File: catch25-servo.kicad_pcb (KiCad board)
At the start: 2 copper layers, 1 part

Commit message: update files
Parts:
- added C1: 10u, Capacitor_SMD:C_0603_1608Metric_Pad1.08x0.95mm_HandSolder, F.Cu at (152.5, 117.5)
- added C2: 22u, Capacitor_SMD:C_0603_1608Metric_Pad1.08x0.95mm_HandSolder, F.Cu at (171.0, 122.5)
- added C3: 10u, Capacitor_SMD:C_0603_1608Metric_Pad1.08x0.95mm_HandSolder, F.Cu at (168.0, 107.0)
- added C4: 10u, Capacitor_SMD:C_0603_1608Metric_Pad1.08x0.95mm_HandSolder, F.Cu at (168.0, 98.5)
- added C5: 0.1u, Capacitor_SMD:C_0603_1608Metric_Pad1.08x0.95mm_HandSolder, F.Cu at (163.0, 97.0)
- added D1: 1N4148, Diode_THT:D_DO-35_SOD27_P7.62mm_Horizontal, F.Cu at (164.5, 106.5)
- added J1: Conn_01x03, Connector_Molex:Molex_SPOX_5268-03A_1x03_P2.50mm_Horizontal, F.Cu at (154.0, 87.6)
- added J2: Conn_01x03, Connector_Molex:Molex_SPOX_5268-03A_1x03_P2.50mm_Horizontal, F.Cu at (165.0, 87.6)
- added J3: Conn_02x05_Odd_Even, Connector_PinSocket_2.54mm:PinSocket_2x05_P2.54mm_Horizontal, F.Cu at (134.4, 85.9)
- added J4: Conn_01x06, Connector_PinSocket_2.54mm:PinSocket_1x06_P2.54mm_Vertical, F.Cu at (131.9, 83.0)
- added J5: Conn_01x02, Connector_AMASS:AMASS_XT30PW-M_1x02_P2.50mm_Horizontal, F.Cu at (158.0, 130.3)
- added Q1: 2N3906, Package_TO_SOT_THT:TO-92_Inline, F.Cu at (157.0, 101.0)
- added R2: 1.2k, Resistor_SMD:R_0603_1608Metric_Pad0.98x0.95mm_HandSolder, F.Cu at (156.5, 109.5)
- added R3: 10k, Resistor_SMD:R_0603_1608Metric_Pad0.98x0.95mm_HandSolder, F.Cu at (158.5, 105.6)
- added R4: 10k, Resistor_SMD:R_0603_1608Metric_Pad0.98x0.95mm_HandSolder, F.Cu at (160.5, 105.6)
- added R5: 10k, Resistor_SMD:R_0603_1608Metric_Pad0.98x0.95mm_HandSolder, F.Cu at (167.3, 95.5)
- added R6: 10k, Resistor_SMD:R_0603_1608Metric_Pad0.98x0.95mm_HandSolder, F.Cu at (167.3, 91.5)
- added R7: 10k, Resistor_SMD:R_0603_1608Metric_Pad0.98x0.95mm_HandSolder, F.Cu at (167.3, 93.5)
- added U1: ~, Package_SO:VSSOP-8_2.3x2mm_P0.5mm, F.Cu at (160.7, 95.0)
- added U2: MC78L05_SOT89, Package_TO_SOT_SMD:SOT-89-3, F.Cu at (169.0, 103.0)
- moved MD1 148.2 mm to (162.0, 118.5), turned to 180 degrees
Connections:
- MD1 pad 1: unconnected-(MD1-~{ON}/OFF_CONTROL-Pad1) -> GND
- MD1 pad 2: unconnected-(MD1-VIN-Pad2) -> +BATT
- MD1 pad 3: unconnected-(MD1-1_GROUND-Pad3) -> GND
- MD1 pad 4: unconnected-(MD1-VOUT-Pad4) -> VCC
- MD1 pad 5: unconnected-(MD1-SENSE-Pad5) -> VCC
- MD1 pad 6: unconnected-(MD1-TRIM-Pad6) -> Net-(MD1-TRIM)
- MD1 pad 7: unconnected-(MD1-2_GROUND-Pad7) -> GND
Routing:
- net +5V: track 0.00 -> 61.2 mm, vias 0 -> 1
- net /UART_TX: track 0.00 -> 51.9 mm, vias 0 -> 2
- net /UART_RX: track 0.00 -> 42.8 mm
- net GND: track 0.00 -> 41.3 mm
- net +BATT: track 0.00 -> 38.3 mm
- net /SERVO_SIG: track 0.00 -> 31.7 mm
- net /TXEN: track 0.00 -> 23.0 mm, vias 0 -> 2
- net VCC: track 0.00 -> 7.72 mm
- net Net-(Q1-B): track 0.00 -> 3.84 mm
- net Net-(MD1-TRIM): track 0.00 -> 3.62 mm
- added copper zone on B.Cu, net GND
- added copper zone on F.Cu, net GND
- added copper zone on B.Cu, net VCC
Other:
- board outline added: 41.5 x 64 mm
- board text added: "FE-IP-1"
- board text added: "IP:192.168."
- board text added: "JLCJLCJLCJLC"

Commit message: update files
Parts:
- added D2: SMAJ45CA, Diode_SMD:D_SMA_Handsoldering, F.Cu at (161.5, 128.0)
- moved C2 3.04 mm to (170.5, 125.5), turned to -90 degrees
- moved J5 1.68 mm to (158.0, 132.0)
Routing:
- net GND: track 41.3 -> 65.8 mm, vias 0 -> 48
- net +BATT: track 38.3 -> 44.8 mm
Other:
- board size 41.5 x 64 mm -> 41.5 x 65 mm

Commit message: update resources
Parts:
- removed U2: MC78L05_SOT89, Package_TO_SOT_SMD:SOT-89-3
- added U3: AMS1117-5.0, Package_TO_SOT_SMD:SOT-223-3_TabPin2, F.Cu at (166.5, 103.0)
- C2: footprint Capacitor_SMD:C_0603_1608Metric_Pad1.08x0.95mm_HandSolder -> Capacitor_SMD:C_0805_2012Metric_Pad1.18x1.45mm_HandSolder
- moved C3 7.65 mm to (160.5, 105.5), turned to -90 degrees
- moved D1 3.03 mm to (162.2, 108.5), turned to 0 degrees
- moved R4 1.51 mm to (159.0, 105.5)
- moved R3 1.01 mm to (157.5, 105.5)
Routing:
- net +5V: track 61.2 -> 75.7 mm
- net +BATT: track 44.8 -> 49.7 mm
- net /UART_TX: track 51.9 -> 50.9 mm
- net GND: vias 48 -> 51

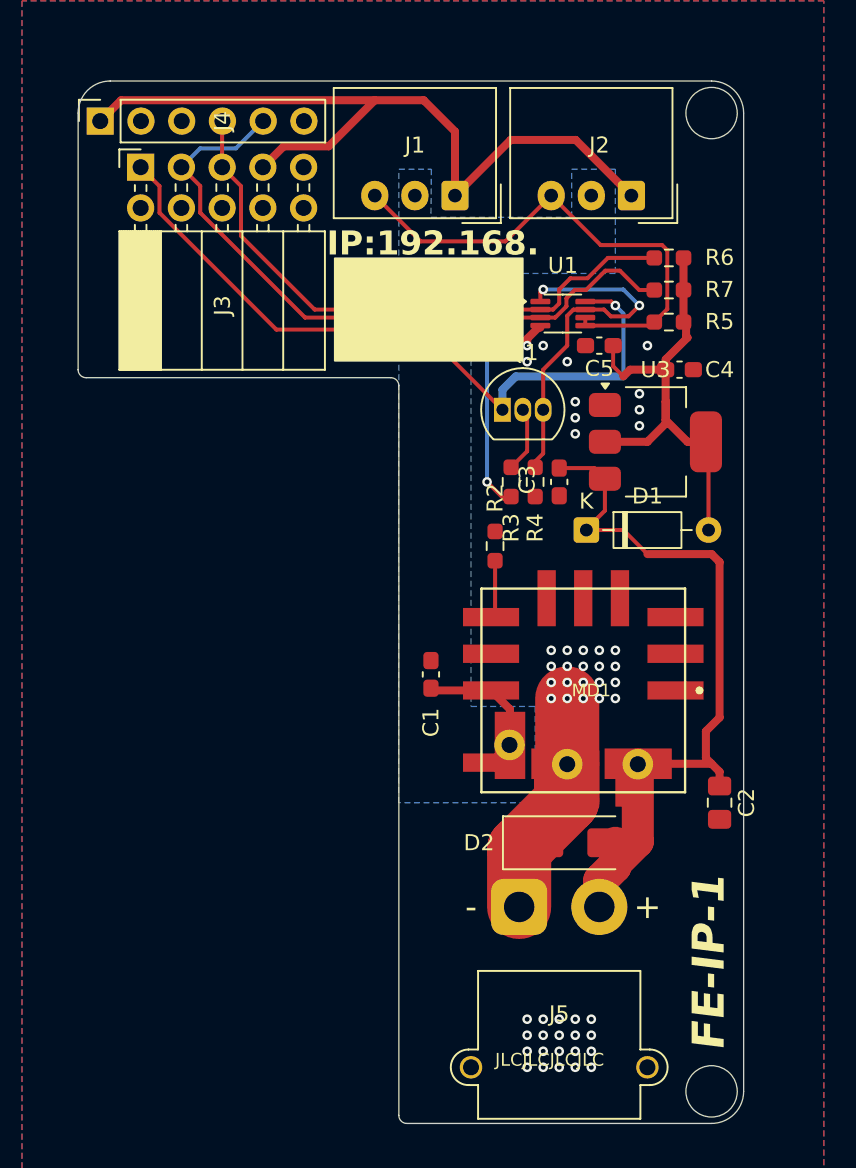
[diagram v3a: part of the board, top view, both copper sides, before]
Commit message: changed okl to breakout board
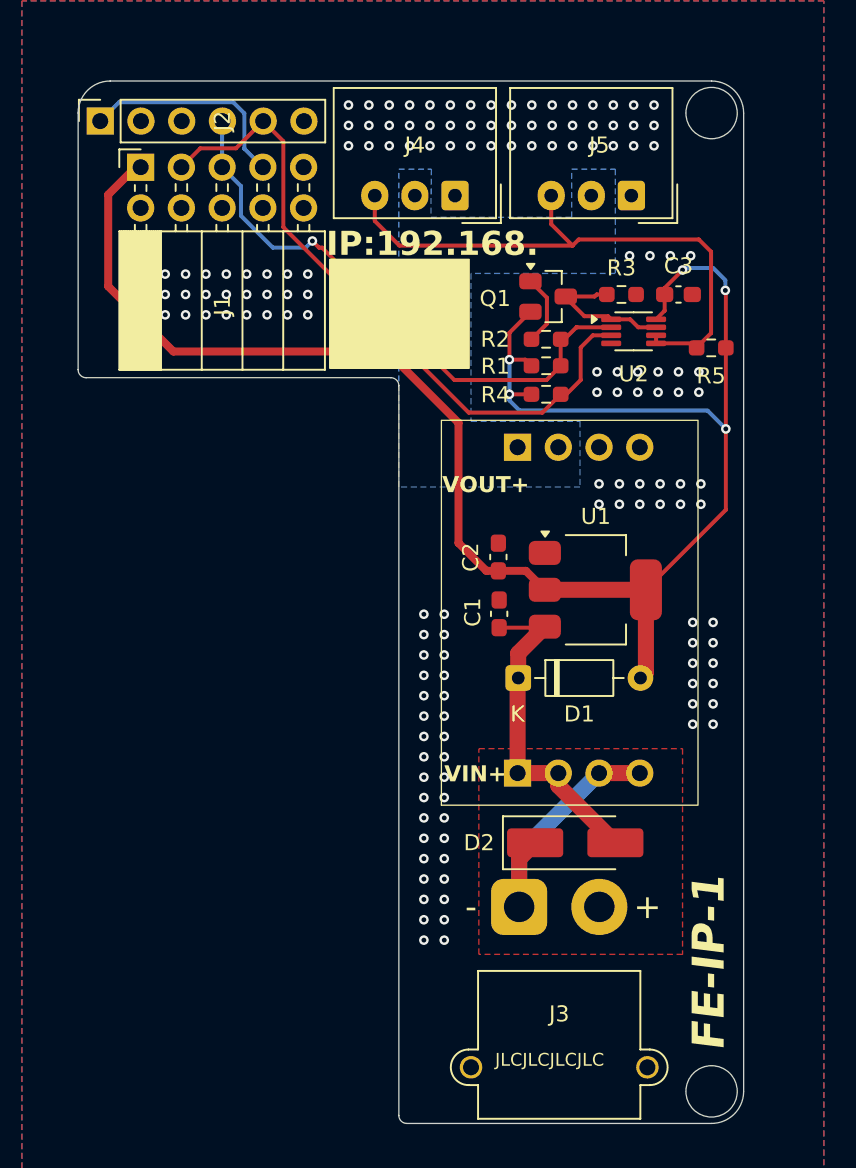
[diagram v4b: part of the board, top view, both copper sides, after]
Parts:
- removed the C1 at (152.5, 117.5)
- removed the C2 at (170.5, 125.5)
- removed MD1: OKL-T_6-W12N-C, Library:MURATA_OKL-T-6-W12N-C_0
- removed the R2 at (156.5, 109.5)
- added U3: ~, Library:OKL, F.Cu at (160.2, 113.7)
- Q1: footprint Package_TO_SOT_THT:TO-92_Inline -> Package_TO_SOT_SMD:SuperSOT-3
- moved C2 16.2 mm to (156.7, 110.2), turned to 90 degrees
- moved R3 12.9 mm to (164.4, 93.8), turned to 180 degrees
- moved R1 10.2 mm to (159.7, 98.3), turned to 180 degrees
- moved D1 10.2 mm to (157.9, 117.7)
- moved R4 10.0 mm to (159.7, 100.0), turned to 180 degrees
- moved U1 9.96 mm to (162.8, 112.2)
- moved R2 9.16 mm to (159.7, 96.6), turned to 180 degrees
- moved C1 9.04 mm to (156.8, 113.7), turned to 90 degrees
- moved Q1 7.61 mm to (159.8, 93.9)
- moved C3 5.88 mm to (167.9, 93.8), turned to 0 degrees
- moved U2 4.55 mm to (165.1, 96.1)
- moved R5 3.09 mm to (170.0, 97.1)
- renumbered C3 to C1, C4 to C2, C5 to C3, J3 to J1, J4 to J2, J5 to J3, J1 to J4, J2 to J5, R6 to R1, R3 to R2, R4 to R3, R7 to R4, U3 to U1, U1 to U2
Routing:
- net +5V: track 75.7 -> 111.2 mm, vias 1 -> 5
- net GND: track 65.8 -> 31.0 mm, vias 51 -> 146
- net +BATT: track 49.7 -> 21.1 mm
- net /UART_TX: track 50.9 -> 36.4 mm, vias 2 -> 1
- net /TXEN: track 22.6 -> 9.08 mm, vias 2 -> 0
- net VCC: track 7.72 -> 0.00 mm
- net /SERVO_SIG: track 31.7 -> 36.8 mm
- net Net-(MD1-TRIM): track 3.62 -> 0.00 mm
- net /UART_RX: track 42.8 -> 41.8 mm
- added copper zone on F.Cu, net +BATT
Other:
- board text added: ". GND RX/IN TX/OUT +5VOUT"
- board text added: ". TX RX . . GND"
- board text added: "Connect RX to converter TX"
- board text added: "Serial Servo IP Interface Board 2025.07 @hirobon1690"
- board text added: "VIN+"
- board text added: "VOUT+"
